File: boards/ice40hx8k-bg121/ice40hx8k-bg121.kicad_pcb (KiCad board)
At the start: 4 copper layers, 22.9 x 48.3 mm, 53 parts, among them J1 BANK 0, J2 BANK 1, J3 BANK 2, J4 BANK 3, U1 AP7361C_SO-8EP, U2 AP7361C_SO-8EP, U3 iCE40HX8K-BG121(121-Ball_caBG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, U4 LE25U20AMB, U5 ASDMB-xxxMHz

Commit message: Send to fab.
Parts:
- added REF**: OSHW-Symbol_6.7x6mm_Copper, Symbol:OSHW-Symbol_6.7x6mm_Copper, B.Cu at (27.2, 32.0)
- turned C18 to 90 degrees
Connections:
- U1 pad 9: (no net) -> GND
- U2 pad 9: (no net) -> GND
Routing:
- net +3V3: track 8.17 -> 39.4 mm, vias 5 -> 13
- net GND: track 15.0 -> 29.1 mm, vias 9 -> 20
- net Net-(D9-Pad1): track 0.00 -> 2.11 mm, vias 0 -> 1
- net Net-(D8-Pad1): track 0.00 -> 2.11 mm, vias 0 -> 1
- net Net-(D7-Pad1): track 0.00 -> 2.11 mm, vias 0 -> 1
- net Net-(D6-Pad1): track 0.00 -> 2.11 mm, vias 0 -> 1
- net Net-(D5-Pad1): track 0.00 -> 2.11 mm, vias 0 -> 1
- net Net-(D4-Pad1): track 0.00 -> 2.11 mm, vias 0 -> 1
- net Net-(D3-Pad1): track 0.00 -> 2.11 mm, vias 0 -> 1
- net Net-(D10-Pad1): track 0.00 -> 2.11 mm, vias 0 -> 1
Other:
- outline, holes or cut-outs redrawn
- rule via_min_size: 0.45 -> 0.23
- board text added: "3V3"
- board text added: "3v3"
- board text added: "5V"
- board text added: "A00"
- board text added: "A01"
- board text added: "A02"
- board text added: "A03"
- board text added: "A04"
- board text added: "A05"
- board text added: "A06"
- board text added: "A07"
- board text added: "A08"
- board text added: "A09"
- board text added: "A10"
- board text added: "A11"
- board text added: "B00"
- board text added: "B01"
- board text added: "B02"
- board text added: "B03"
- board text added: "B04"
- board text added: "B05"
- board text added: "B06"
- board text added: "C00"
- board text added: "C01"
- board text added: "C02"
- board text added: "C03"
- board text added: "C04"
- board text added: "C05"
- board text added: "C06"
- board text added: "C07"
- board text added: "CRESET_B"
- board text added: "D00"
- board text added: "D01"
- board text added: "D02"
- board text added: "D03"
- board text added: "D04"
- board text added: "D05"
- board text added: "D06"
- board text added: "GND"
- board text added: "L0"
- board text added: "L1"
- board text added: "L2"
- board text added: "L3"
- board text added: "L4"
- board text added: "L5"
- board text added: "L6"
- board text added: "L7"
- board text added: "SCK"
- board text added: "SDI"
- board text added: "SDO"
- board text added: "VIO A"
- board text added: "VIO B"
- board text added: "VIO C"
- board text added: "VIO D"
- board text added: "fourside.io ice40hx8k breakout 2020-01"
- board text removed: "Oh yeah, this thing can be like 1.5-2x long."

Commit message: Updated LDOs to SOT89-5 footprint.
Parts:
- removed D1: 1V2_5V, Diode_SMD:D_0805_2012Metric
- removed D2: 1V2_3V3, Diode_SMD:D_0805_2012Metric
- removed REF**: OSHW-Symbol_6.7x6mm_Copper, Symbol:OSHW-Symbol_6.7x6mm_Copper
- U1: value AP7361C_SO-8EP -> AP7361C-33Y5-13; footprint Package_SO:Diodes_SO-8EP -> jkiv-library:SOT89-5
- U2: value AP7361C_SO-8EP -> AP7361C-12Y5-13; footprint Package_SO:Diodes_SO-8EP -> jkiv-library:SOT89-5
- moved R1 2.96 mm to (27.9, 17.8), turned to 0 degrees
- moved C3 2.54 mm to (35.1, 19.8)
- moved C1 2.48 mm to (27.9, 19.8)
- moved C2 2.48 mm to (27.9, 21.8), turned to 180 degrees
- moved R2 1.98 mm to (35.1, 17.8), turned to 0 degrees
- moved C4 1.56 mm to (35.1, 21.8), turned to 180 degrees
- moved U1 0.78 mm to (27.9, 20.0), turned to 180 degrees
- moved U2 0.52 mm to (35.1, 20.0), turned to 180 degrees
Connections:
- C3 pad 1: Net-(C3-Pad1) -> +5V
- R2 pad 1: Net-(C3-Pad1) -> +5V
- U1 pad 1: +3V3 -> Net-(R1-Pad2)
- U1 pad 2: Net-(R1-Pad2) -> GND
- U1 pad 4: GND -> +5V
- U1 pad 5: Net-(U1-Pad3) -> +3V3
- U2 pad 1: +1V2 -> Net-(R2-Pad2)
- U2 pad 2: Net-(R2-Pad2) -> GND
- U2 pad 4: GND -> +5V
- U2 pad 5: Net-(U2-Pad3) -> +1V2
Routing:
- net Net-(C3-Pad1): track 19.5 -> 0.00 mm, vias 1 -> 0
- net GND: track 29.1 -> 11.9 mm, vias 20 -> 7
- net +3V3: track 39.4 -> 32.2 mm, vias 13 -> 12
- net +5V: track 5.38 -> 9.85 mm, vias 1 -> 4
- net Net-(R2-Pad2): track 5.69 -> 3.24 mm
- added copper zone on B.Cu, net +1V2
- added copper zone on B.Cu, net +3V3
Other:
- board text added: "fourside.io ice40hx8k breakout 2020-02"
- board text removed: "fourside.io ice40hx8k breakout 2020-01"

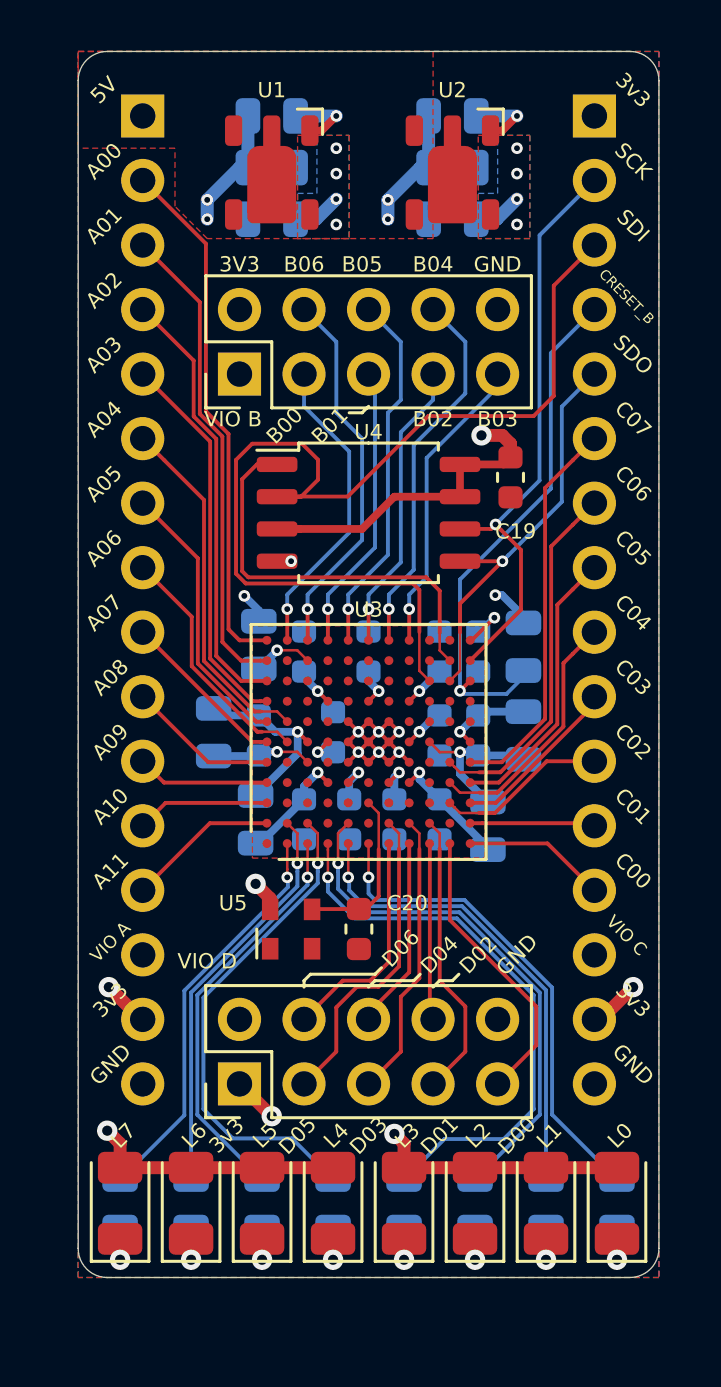
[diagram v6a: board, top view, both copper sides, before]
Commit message: Fixed programming CRESET_B/SPI_SS_B. Fixed ground connections. Fixed 2V5.
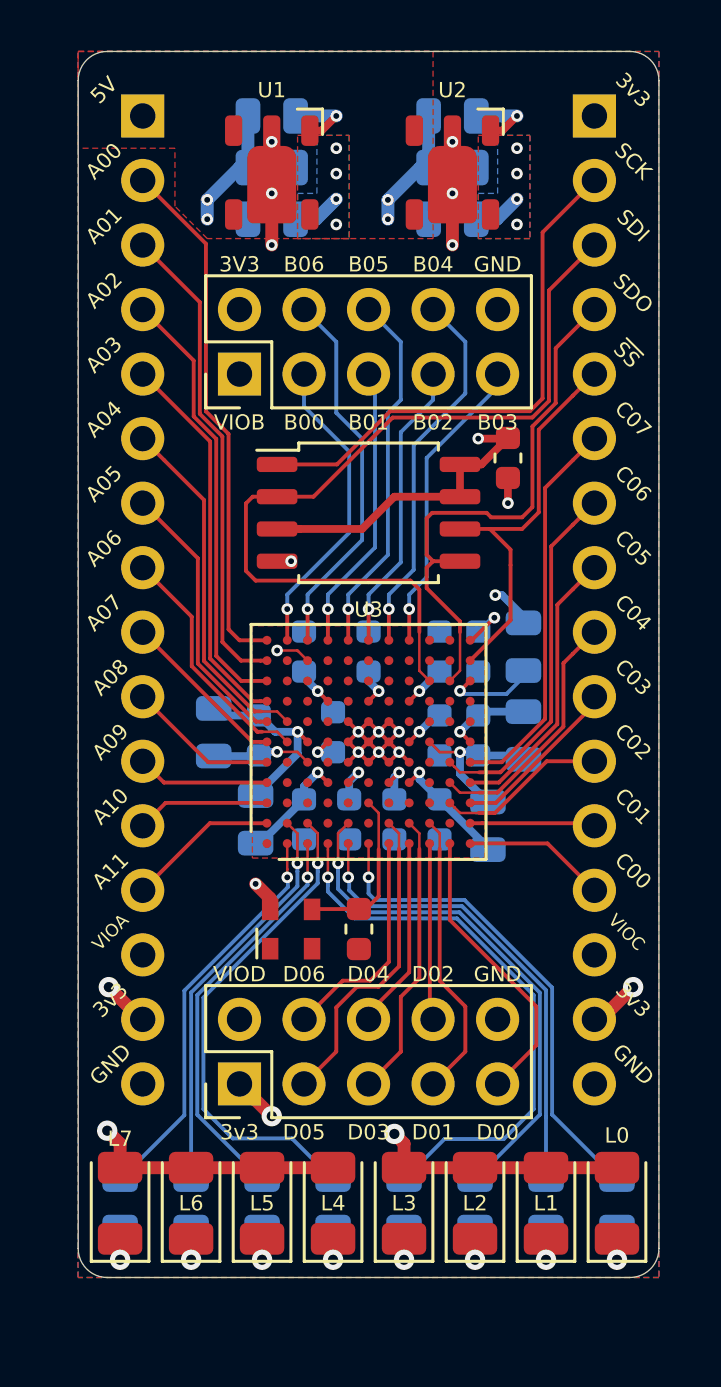
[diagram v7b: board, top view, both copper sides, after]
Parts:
- removed D11: D_Schottky, Diode_SMD:D_0805_2012Metric
- moved C19 0.77 mm to (37.2, 31.2)
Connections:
- J2 pad 2: PROG_SCK -> PROG_SS_B
- J2 pad 4: PROG_CRESET_B -> PROG_SDO
- J2 pad 5: PROG_SDO -> PROG_SCK
- U3 pad C10: Net-(D11-Pad1) -> +3V3
- U3 pad K10: PROG_SS_B -> Net-(U3-PadK10)
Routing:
- net PROG_CRESET_B: track 21.0 -> 3.75 mm
- net PROG_SCK: track 23.2 -> 15.9 mm, vias 1 -> 0
- net PROG_SDI: track 41.3 -> 34.0 mm
- net GND: track 11.9 -> 17.7 mm, vias 7 -> 14
- net PROG_SDO: track 16.1 -> 21.7 mm, vias 1 -> 0
- net PROG_SS_B: track 16.2 -> 21.0 mm
- net Net-(D11-Pad1): track 2.40 -> 0.00 mm, vias 1 -> 0
- net +3V3: track 32.2 -> 34.2 mm
- net VCCIO_C: track 43.2 -> 42.6 mm
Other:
- board text added: "VIOA"
- board text added: "VIOB"
- board text added: "VIOC"
- board text added: "VIOD"
- board text added: "~SS"
- board text removed: "CRESET_B"
- board text removed: "VIO A"
- board text removed: "VIO B"
- board text removed: "VIO C"
- board text removed: "VIO D"

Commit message: Silkscreen fixes. Moved C19.
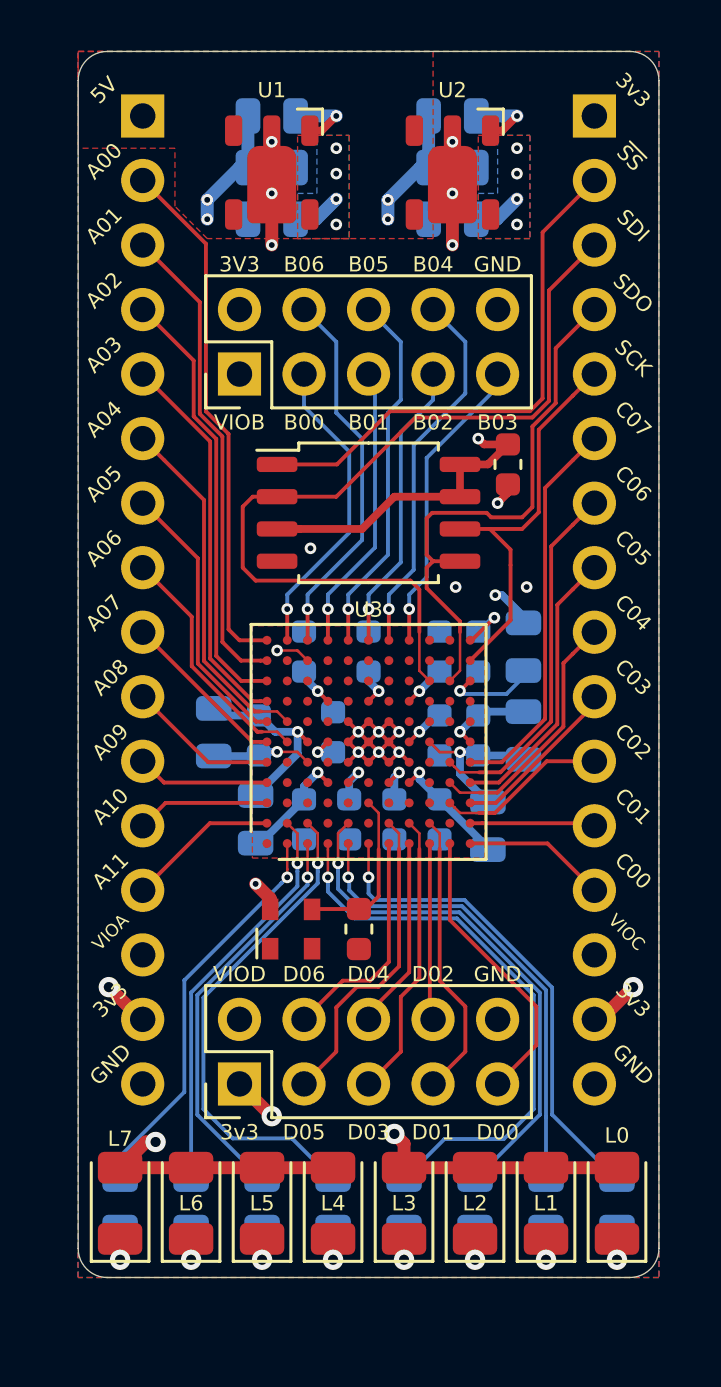
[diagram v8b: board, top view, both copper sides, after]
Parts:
- added REF**: OSHW-Symbol_6.7x6mm_SilkScreen, Symbol:OSHW-Symbol_6.7x6mm_SilkScreen, B.Cu at (31.8, 33.0)
- moved C19 0.25 mm to (37.2, 31.5)
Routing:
- net GND: track 17.7 -> 17.6 mm, vias 14 -> 16
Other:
- board text added: "ice40hx8k breakout 2020-03 fourside.io"
- board text removed: "fourside.io ice40hx8k breakout 2020-02"
